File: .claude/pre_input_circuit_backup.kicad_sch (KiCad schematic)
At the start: 64 parts, among them J1 USB_C_Receptacle_USB2.0_16P, J10 5055670271, J2 5055670271, J3 SM04B-GHS-TB, J4 XT30 (right-angle), J5 SM04B-GHS-TB, J6 5055670271, J7 5055670271, J8 5055670271, J9 5055670271, Q1 DMP3098L-7, SW1 SW_Push, SW2 SW_Push, U1 USBLC6-2SC6, U2 AMS1117-3.3, U3 ESP32-S3-WROOM-1, U4 TJA1051T/3, U5 AP3602A, U6 LMR33630

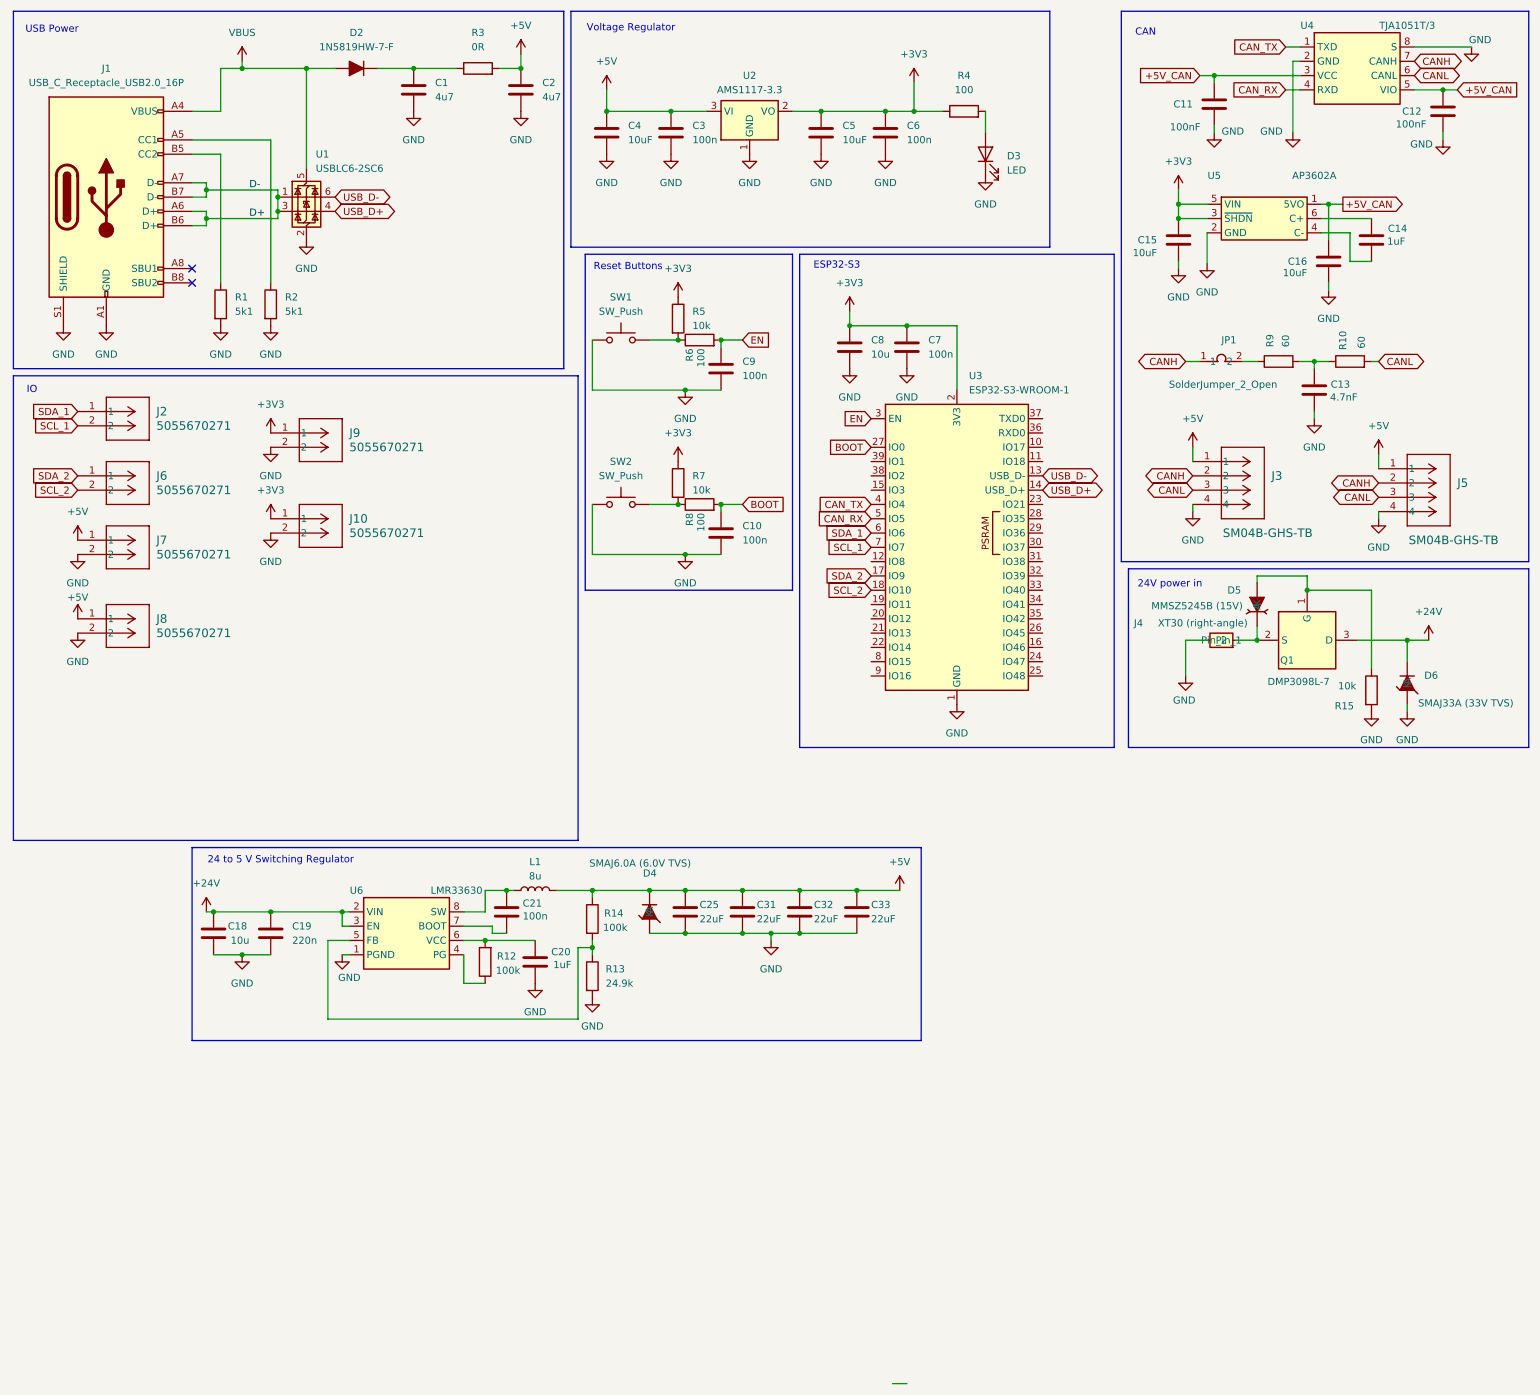
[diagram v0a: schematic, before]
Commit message: Complete minimal IO. Need Bulk IO connector
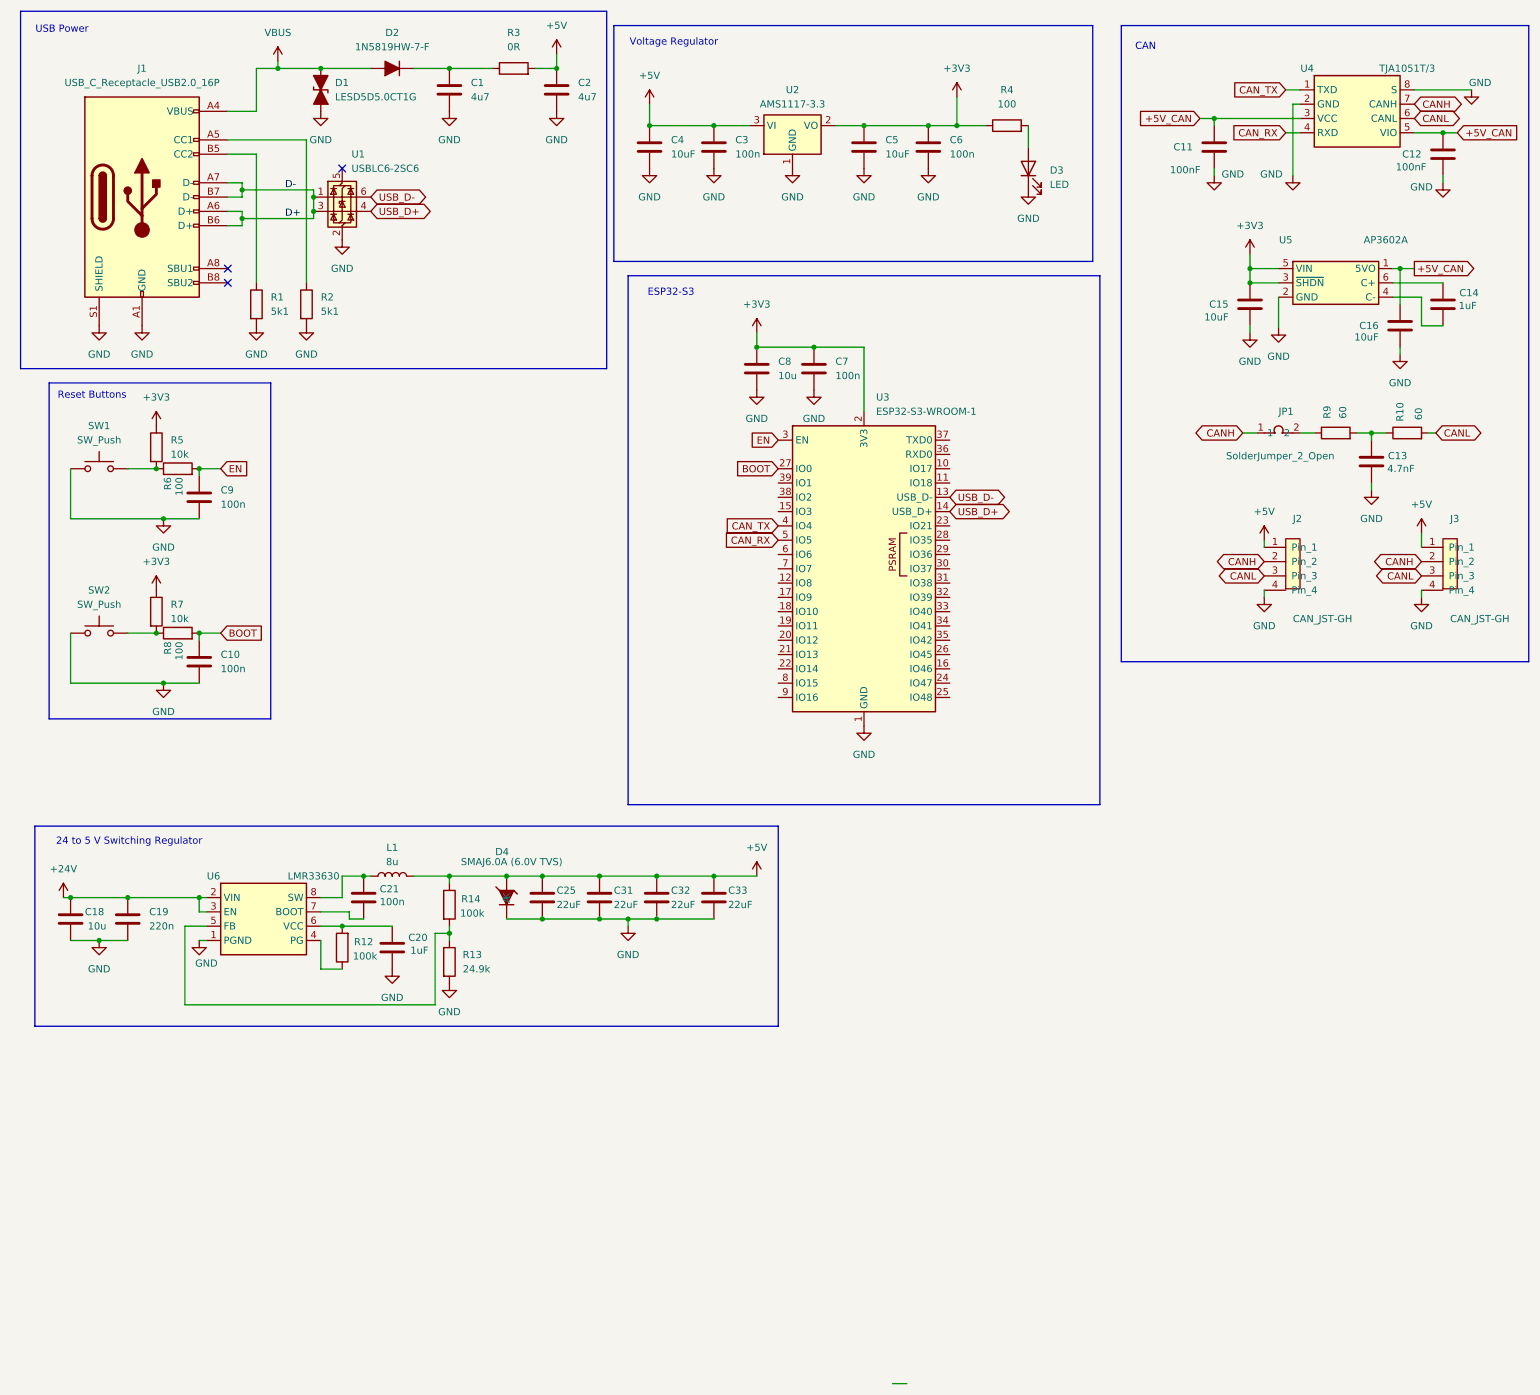
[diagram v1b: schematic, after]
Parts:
- removed D5: MMSZ5245B (15V), Diode_SMD:D_SOD-123, symbol Device:D_Zener
- removed D6: SMAJ33A (33V TVS), Diode_SMD:D_SMA, symbol Device:D_TVS
- removed J10, J2, J6, J7, J8, J9: 5055670271, CONN_505567_02_MOL, symbol 2026-07-21_10-18-21:5055670271
- removed J3, J5: SM04B-GHS-TB, CONN_SM04B-GHS-TB_JST, symbol 2026-07-21_10-23-02:SM04B-GHS-TB
- removed J4: XT30 (right-angle), Connector_AMASS:AMASS_XT30PW-F_1x02_P2.50mm_Horizontal, symbol Connector_Generic:Conn_01x02
- removed Q1: DMP3098L-7, Package_TO_SOT_SMD:SOT-23, symbol Transistor_FET:DMP3098L
- removed R15: 10k, Resistor_SMD:R_0402_1005Metric, symbol Device:R
- added D1: LESD5D5.0CT1G, Diode_SMD:D_SOD-523, symbol Device:D_TVS_Filled
- added J2, J3: CAN_JST-GH, Connector_JST:JST_GH_SM04B-GHS-TB_1x04-1MP_P1.25mm, symbol Connector_Generic:Conn_01x04
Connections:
- net +5V: now also D4.2 (A), J2.1 (Pin_1), J3.1 (Pin_1); no longer D4.1 (K)
- net CANH: now also J2.2 (Pin_2), J3.2 (Pin_2)
- net CANL: now also J2.3 (Pin_3), J3.3 (Pin_3)
- net GND: now also D4.1 (K), D1.1 (A1), J2.4 (Pin_4), J3.4 (Pin_4); no longer D4.2 (A)
- net VBUS: now also D1.2 (A2); no longer U1.5 (VBUS)
- net SCL_1: no longer names the net of U3.7 (IO7)
- net SCL_2: no longer names the net of U3.18 (IO10)
- net SDA_1: no longer names the net of U3.6 (IO6)
- net SDA_2: no longer names the net of U3.17 (IO9)
- no-connect marks 2 -> 3
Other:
- note removed: "24V power in"
- note removed: "IO"
- moved on the sheet: C1, C10, C11, C12, C13, C14, C15, C16, C18, C19, C2, C20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
